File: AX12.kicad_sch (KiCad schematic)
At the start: 6 parts, among them J25 Conn_AX12, U5 74LVC2G241

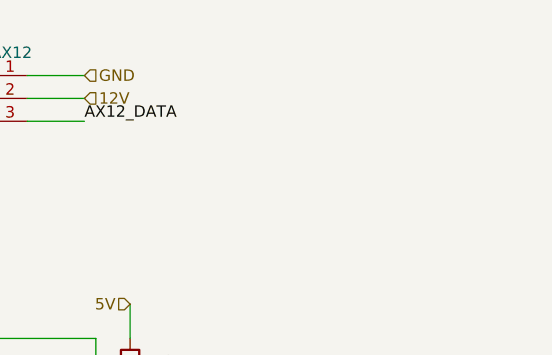
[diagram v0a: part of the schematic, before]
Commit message: add second AX12 connector + change stepper connectors + add 12V connector. Todo : add SPI for RFID
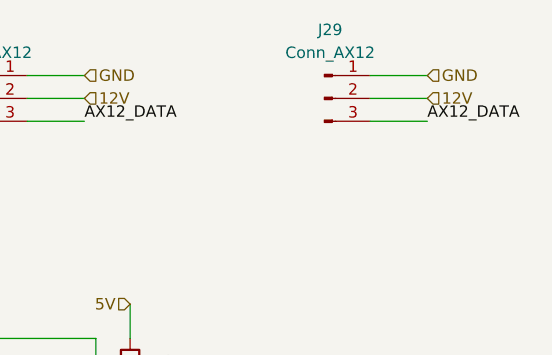
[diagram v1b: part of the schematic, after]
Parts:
- added J29: Conn_AX12, Connector_JST:JST_XH_B3B-XH-A_1x03_P2.50mm_Vertical, symbol Connector:Conn_01x03_Male
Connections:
- net 12V: now also J29.2 (Pin_2)
- net AX12_DATA: now also J29.3 (Pin_3)
- net GND: now also J29.1 (Pin_1)
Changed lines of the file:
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@@
+    (stroke (width 0) (type default) (color 0 0 0 0))
+  )
+  (wire (pts (xy 153.67 68.58) (xy 147.32 68.58))
     (stroke (width 0) (type default) (color 0 0 0 0))
   )
@@
     (stroke (width 0) (type default) (color 0 0 0 0))
   )
+  (wire (pts (xy 153.67 66.04) (xy 147.32 66.04))
+    (stroke (width 0) (type default) (color 0 0 0 0))
+  )
+  (wire (pts (xy 153.67 71.12) (xy 147.32 71.12))
+    (stroke (width 0) (type default) (color 0 0 0 0))
+  )
   (wire (pts (xy 97.79 110.49) (xy 116.84 110.49))
     (stroke (width 0) (type default) (color 0 0 0 0))
@@
     (effects (font (size 1.27 1.27)) (justify left bottom))
   )
+  (label "AX12_DATA" (at 153.67 71.12 0)
+    (effects (font (size 1.27 1.27)) (justify left bottom))
+  )
   (hierarchical_label "5V" (shape input) (at 113.03 114.3 0)
     (effects (font (size 1.27 1.27)) (justify left))
@@
   (hierarchical_label "5V" (shape input) (at 77.47 86.36 180)
     (effects (font (size 1.27 1.27)) (justify right))
+  )
+  (hierarchical_label "12V" (shape input) (at 153.67 68.58 0)
+    (effects (font (size 1.27 1.27)) (justify left))
   )
   (hierarchical_label "5V" (shape input) (at 92.71 106.68 0)
@@
   )
   (hierarchical_label "GND" (shape input) (at 102.87 102.87 0)
+    (effects (font (size 1.27 1.27)) (justify left))
+  )
+  (hierarchical_label "GND" (shape input) (at 153.67 66.04 0)
     (effects (font (size 1.27 1.27)) (justify left))
   )
@@
       (effects (font (size 1.27 1.27)) hide)
     )
+    (pin "1")
+    (pin "2")
+    (pin "3")
+  )
+  (symbol (lib_id "Connector:Conn_01x03_Male") (at 142.24 68.58 0) (unit 1)
+    (in_bom yes) (on_board yes) (fields_autoplaced)
+    (property "Reference" "J29" (id 0) (at 142.875 60.96 0))
+    (property "Value" "Conn_AX12" (id 1) (at 142.875 63.5 0))
+    (property "Footprint" "Connector_JST:JST_XH_B3B-XH-A_1x03_P2.50mm_Vertical" (id 2) (at 142.24 68.58 0)
+      (effects (font (size 1.27 1.27)) hide)
+    )
+    (property "Datasheet" "~" (id 3) (at 142.24 68.58 0)
+      (effects (font (size 1.27 1.27)) hide)
+    )

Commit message: Add SPI connector + route control pins (LEDs, AX12)
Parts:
- R22, R23, R24: footprint Resistor_SMD:R_0805_2012Metric -> Resistor_SMD:R_0603_1608Metric
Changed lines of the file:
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@@
       (effects (font (size 1.27 1.27)) (justify left))
     )
-    (property "Footprint" "Resistor_SMD:R_0805_2012Metric" (id 2) (at 78.232 91.44 90)
+    (property "Footprint" "Resistor_SMD:R_0603_1608Metric" (id 2) (at 78.232 91.44 90)
       (effects (font (size 1.27 1.27)) hide)
     )
@@
     (property "Reference" "R23" (id 0) (at 95.25 96.52 90))
     (property "Value" "10k" (id 1) (at 95.25 99.06 90))
-    (property "Footprint" "Resistor_SMD:R_0805_2012Metric" (id 2) (at 95.25 104.648 90)
+    (property "Footprint" "Resistor_SMD:R_0603_1608Metric" (id 2) (at 95.25 104.648 90)
       (effects (font (size 1.27 1.27)) hide)
     )
@@
     (pin "4")
     (pin "8")
-    (pin "1")
-    (pin "2")
-    (pin "6")
     (pin "3")
     (pin "5")
@@
     (pin "2")
     (pin "6")
-    (pin "3")
-    (pin "5")
-    (pin "7")
   )
   (symbol (lib_id "Device:R") (at 120.65 99.06 0) (unit 1)
@@
       (effects (font (size 1.27 1.27)) (justify left))
     )
-    (property "Footprint" "Resistor_SMD:R_0805_2012Metric" (id 2) (at 118.872 99.06 90)
+    (property "Footprint" "Resistor_SMD:R_0603_1608Metric" (id 2) (at 118.872 99.06 90)
       (effects (font (size 1.27 1.27)) hide)
     )

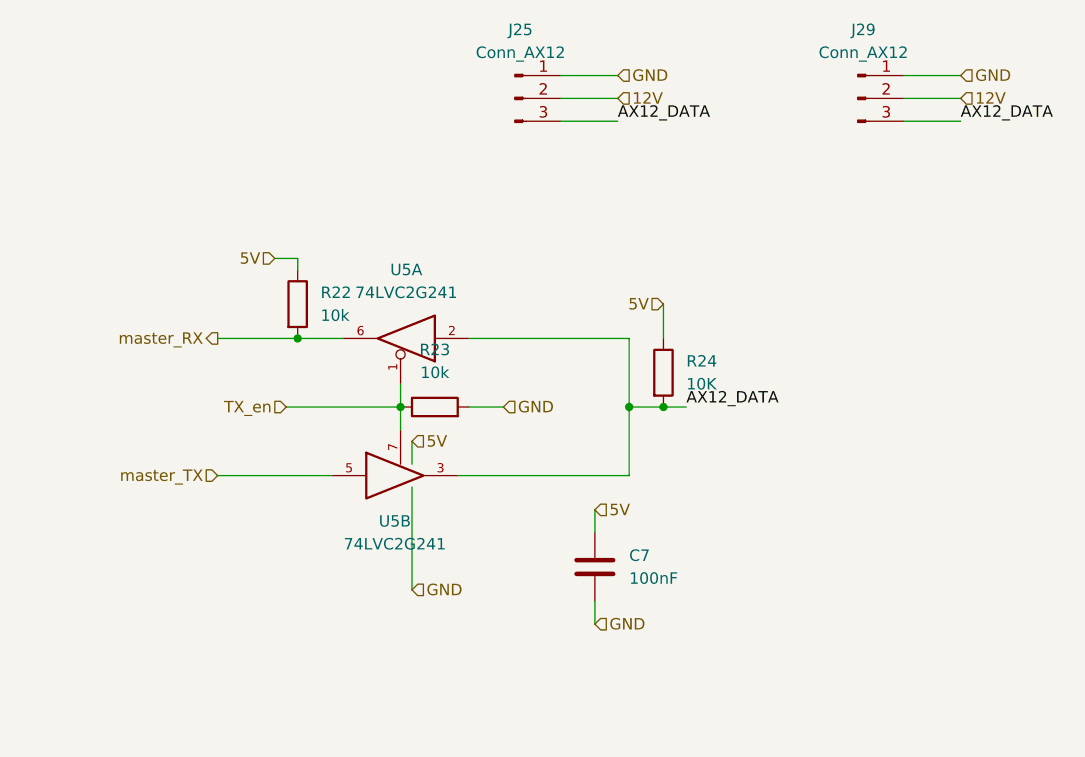
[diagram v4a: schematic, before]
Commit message: remove intra-board zeners
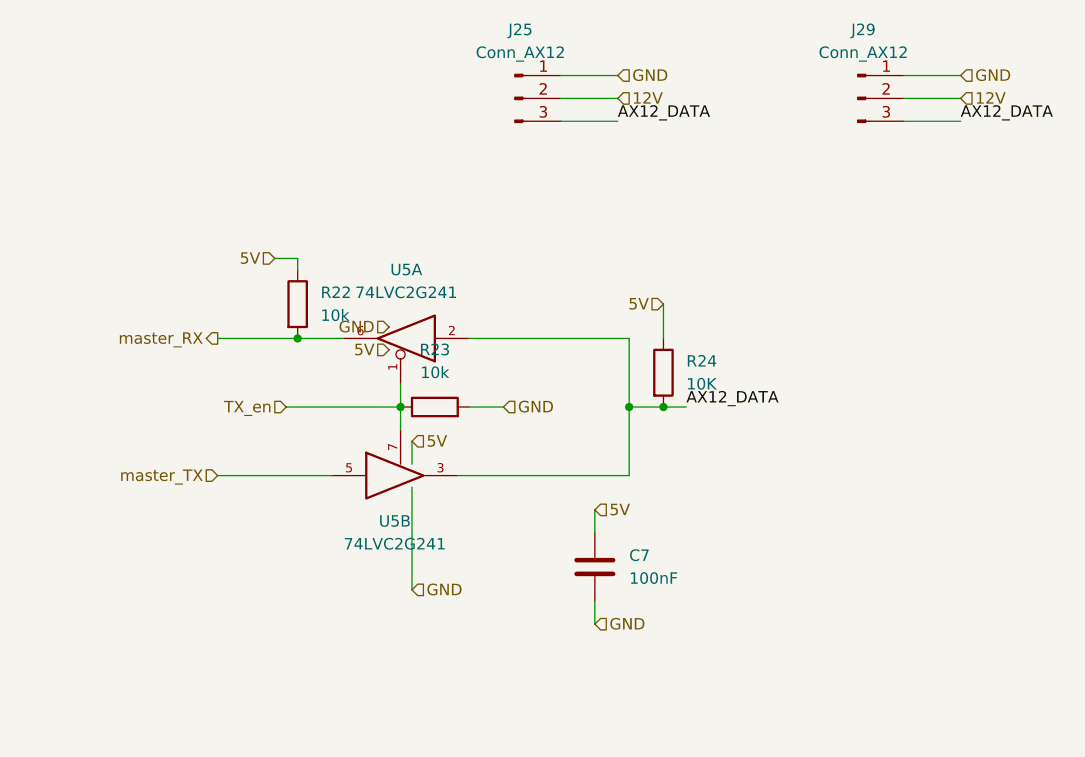
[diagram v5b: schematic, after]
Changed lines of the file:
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@@
+		)
+	)
+	(hierarchical_label "5V"
+		(shape input)
+		(at 90.17 96.52 180)
+		(fields_autoplaced yes)
+		(effects
+			(font
+				(size 1.27 1.27)
+			)
+			(justify right)
 		)
 	)
@@
 		(fields_autoplaced yes)
 		(effects
+			(font
+				(size 1.27 1.27)
+			)
+			(justify right)
+		)
+	)
+	(hierarchical_label "GND"
+		(shape input)
+		(at 90.17 93.98 180)
+		(fields_autoplaced yes)
+		(effects

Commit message: fix warnings + add internal layers + add Uart to steppers (TX only
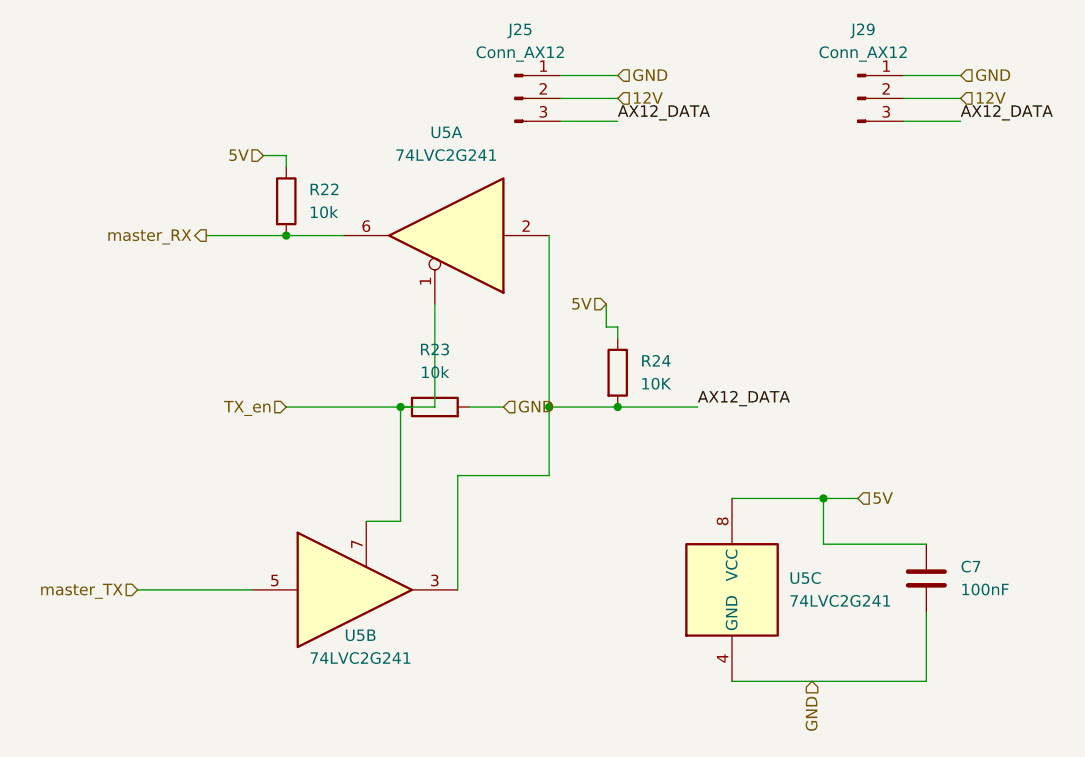
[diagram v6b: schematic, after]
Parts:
- added unit 3 of U5
- J25, J29: symbol Connector:Conn_01x03_Male -> Connector:Conn_01x03_Pin
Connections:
- net GND: now also U5.4 (GND); no longer U5.4 (GND), U5.4 (GND)
- net VCC renamed 5V
- net 5V: now also U5.8 (VCC); no longer U5.8 (VCC), U5.8 (VCC)
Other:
- moved on the sheet: R22, R24

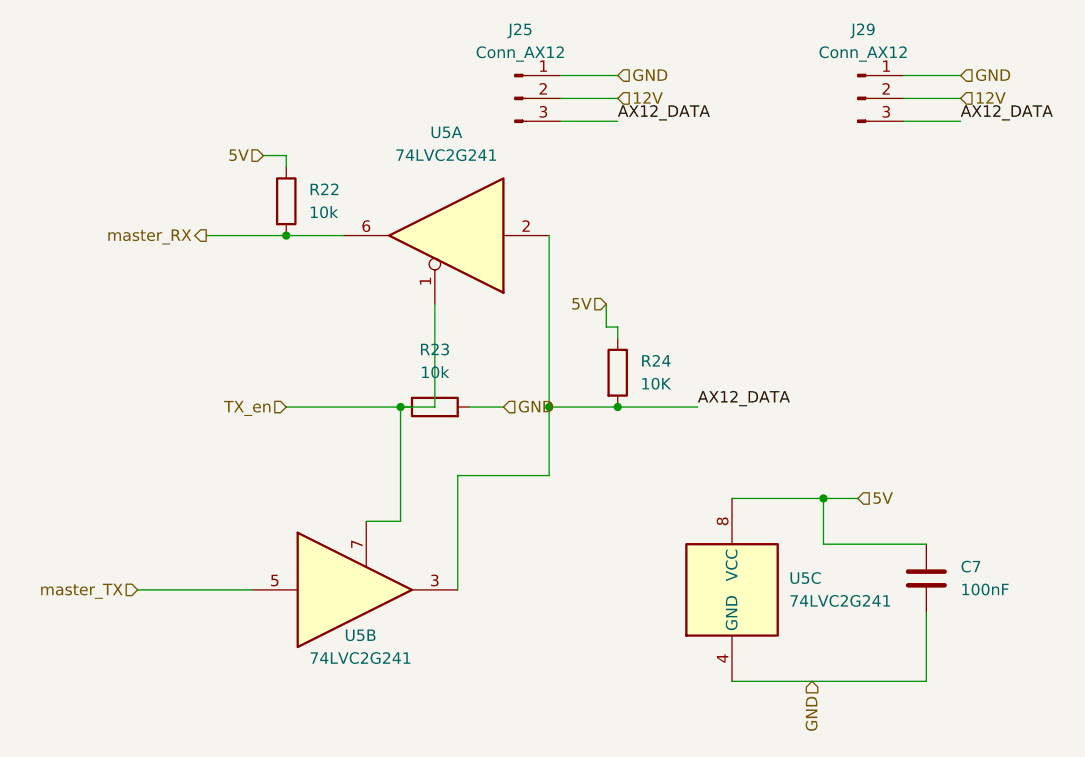
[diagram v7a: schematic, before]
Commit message: Add BOM
Add LCSC reference and correct few footprint acording bom
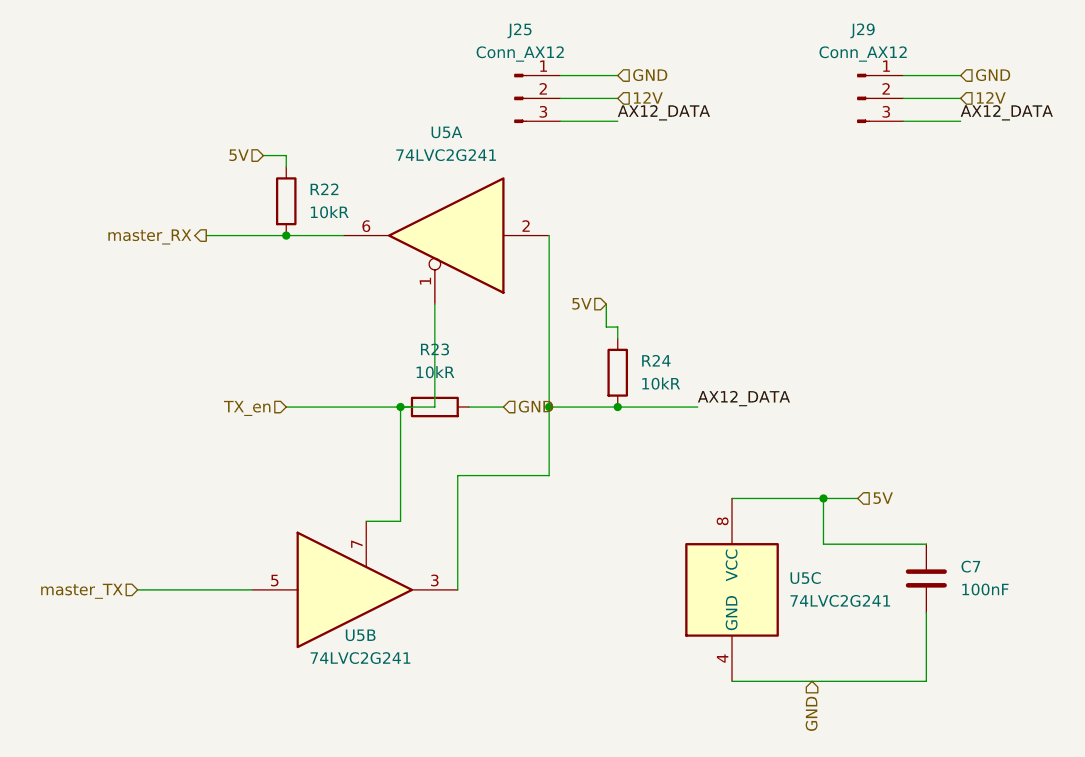
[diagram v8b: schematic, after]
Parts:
- C7: footprint Capacitor_SMD:C_0805_2012Metric -> Capacitor_SMD:C_0603_1608Metric; LCSC# (none) -> C14663
- J25, J29: LCSC# (none) -> C144394
- R22, R23: value 10k -> 10kR; LCSC# (none) -> C2930027
- R24: value 10K -> 10kR; LCSC# (none) -> C2930027
- U5: LCSC# (none) -> C10430; Mouser https://www.mouser.fr/ProductDetail/Texas-Instruments/SN74L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 -> (none)
- U5: LCSC# (none) -> C10430
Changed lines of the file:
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@@
 	(label "AX12_DATA"
 		(at 115.57 71.12 0)
-		(fields_autoplaced yes)
 		(effects
 			(font
@@
 	(label "AX12_DATA"
 		(at 124.46 102.87 0)
-		(fields_autoplaced yes)
 		(effects
 			(font
@@
 	(label "AX12_DATA"
 		(at 153.67 71.12 0)
-		(fields_autoplaced yes)
 		(effects
 			(font
@@
 		(shape input)
 		(at 137.16 133.35 270)
-		(fields_autoplaced yes)
 		(effects
 			(font
@@
 		(shape input)
 		(at 142.24 113.03 0)
-		(fields_autoplaced yes)
 		(effects
 			(font
@@
 		(shape input)
 		(at 76.2 74.93 180)
-		(fields_autoplaced yes)
 		(effects
 			(font
@@
 		(shape input)
 		(at 153.67 68.58 0)
-		(fields_autoplaced yes)
 		(effects
 			(font
@@
 		(shape input)
 		(at 114.3 91.44 180)
-		(fields_autoplaced yes)
 		(effects
 			(font
@@
 		(shape input)
 		(at 115.57 68.58 0)
-		(fields_autoplaced yes)
 		(effects
 			(font
@@
 		(shape output)
 		(at 69.85 83.82 180)
-		(fields_autoplaced yes)
 		(effects
 			(font
@@
 		(shape input)
 		(at 115.57 66.04 0)
-		(fields_autoplaced yes)
 		(effects
 			(font
@@
 		(shape input)
 		(at 102.87 102.87 0)
-		(fields_autoplaced yes)
 		(effects
 			(font
@@
 		(shape input)
 		(at 153.67 66.04 0)
-		(fields_autoplaced yes)
 		(effects
 			(font
@@
 		(shape input)
 		(at 78.74 102.87 180)
-		(fields_autoplaced yes)
 		(effects
 			(font
@@
 		(shape input)
 		(at 62.23 123.19 180)
-		(fields_autoplaced yes)
 		(effects
 			(font
@@
 			)
 		)
-		(property "Mouser" "https://www.mouser.fr/ProductDetail/Texas-Instruments/SN74LVC2G241DCUR?qs=JS6RUWRH9DV7W1UO8b3P2w%3D%3D"
+		(property "LCSC#" "C10430"
 			(at 128.27 123.19 0)
 			(effects
@@
 			)
 		)
+		(property "LCSC#" "C144394"
+			(at 104.14 68.58 0)
+			(effects
+				(font
+					(size 1.27 1.27)
+				)
+				(hide yes)
+			)
+		)
 		(pin "1"
 		)
@@
 			)
 		)
+		(property "LCSC#" "C144394"
+			(at 142.24 68.58 0)
+			(effects
+				(font
+					(size 1.27 1.27)
+				)
+				(hide yes)
+			)
+		)
 		(pin "1"
 		)
@@
 			)
 		)
-		(property "Value" "10k"
+		(property "Value" "10kR"
 			(at 81.28 81.2799 0)
 			(effects
@@
 		)
 		(property "Description" ""
+			(at 78.74 80.01 0)
+			(effects
+				(font
+					(size 1.27 1.27)
+				)
+				(hide yes)
+			)
+		)
+		(property "LCSC#" "C2930027"
 			(at 78.74 80.01 0)
 			(effects
@@
 			)
 		)
-		(property "Value" "10k"
+		(property "Value" "10kR"
 			(at 95.25 99.06 90)
 			(effects
@@
 		)
 		(property "Description" ""
+			(at 95.25 102.87 0)
+			(effects
+				(font
+					(size 1.27 1.27)
+				)
+				(hide yes)
+			)
+		)
+		(property "LCSC#" "C2930027"
 			(at 95.25 102.87 0)
 			(effects
@@
 			)
 		)
-		(property "Mouser" "https://www.mouser.fr/ProductDetail/Texas-Instruments/SN74LVC2G241DCUR?qs=JS6RUWRH9DV7W1UO8b3P2w%3D%3D"
+		(property "LCSC#" "C10430"
 			(at 87.63 123.19 0)
 			(effects
@@
 			)
 		)
-		(property "Footprint" "Capacitor_SMD:C_0805_2012Metric"
+		(property "Footprint" "Capacitor_SMD:C_0603_1608Metric"
 			(at 150.8252 125.73 0)
 			(effects
@@
 		)
 		(property "Description" ""
+			(at 149.86 121.92 0)
+			(effects
+				(font
+					(size 1.27 1.27)
+				)
+				(hide yes)
+			)
+		)
+		(property "LCSC#" "C14663"
 			(at 149.86 121.92 0)
 			(effects
@@
 			)
 		)
+		(property "LCSC#" "C10430"
+			(at 95.25 83.82 0)
+			(effects
+				(font
+					(size 1.27 1.27)
+				)
+				(hide yes)
+			)
+		)
 		(pin "4"
 		)
@@
 			)
 		)
-		(property "Value" "10K"
+		(property "Value" "10kR"
 			(at 118.11 100.3299 0)
 			(effects
@@
 			(at 115.57 99.06 0)
 			(effects
+				(font
+					(size 1.27 1.27)
+				)
+				(hide yes)
+			)
+		)
+		(property "LCSC#" "C2930027"
+			(at 115.57 99.06 0)
+			(effects
